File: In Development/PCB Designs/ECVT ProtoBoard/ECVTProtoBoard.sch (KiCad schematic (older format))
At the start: 26 parts, among them J1 Motor Driver, J10 3V3, J11 GND, J12 Hall Effect, J13 Hall Effect 2, J14 12V In, J15 Conn_01x08, J16 MotorDriver2, J17 GND In, J2 Conn_01x01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

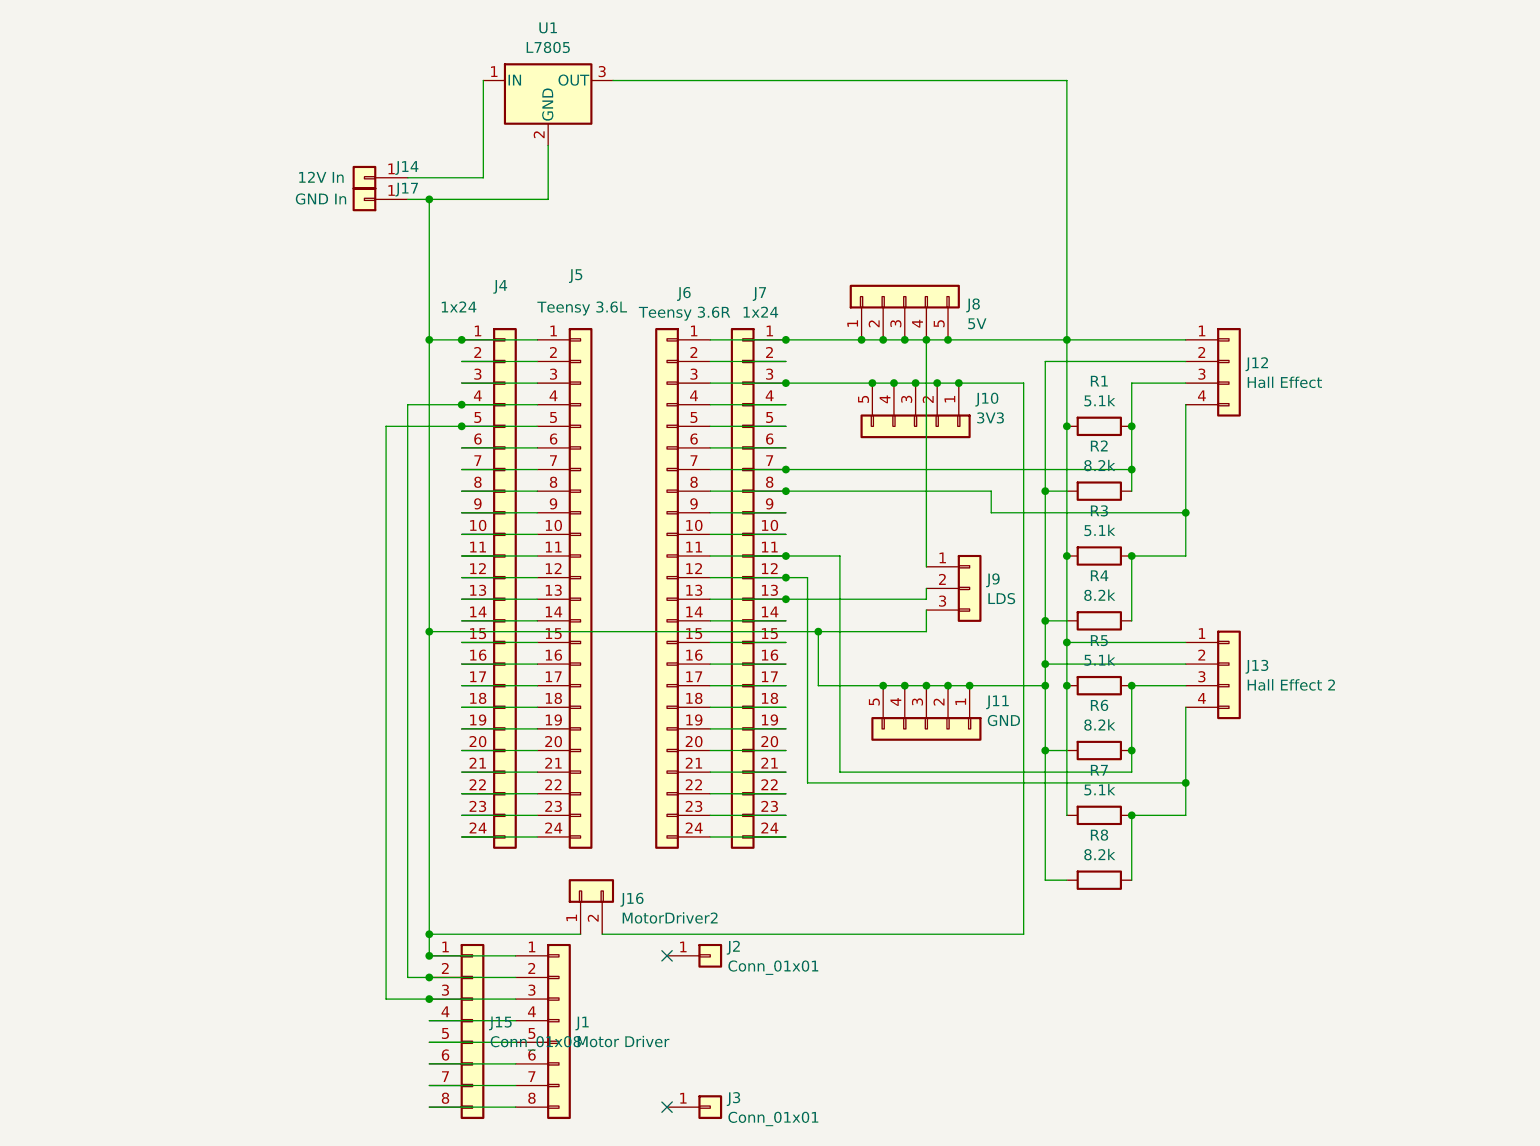
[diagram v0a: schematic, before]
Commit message: Finished eCVT protoboard schematic
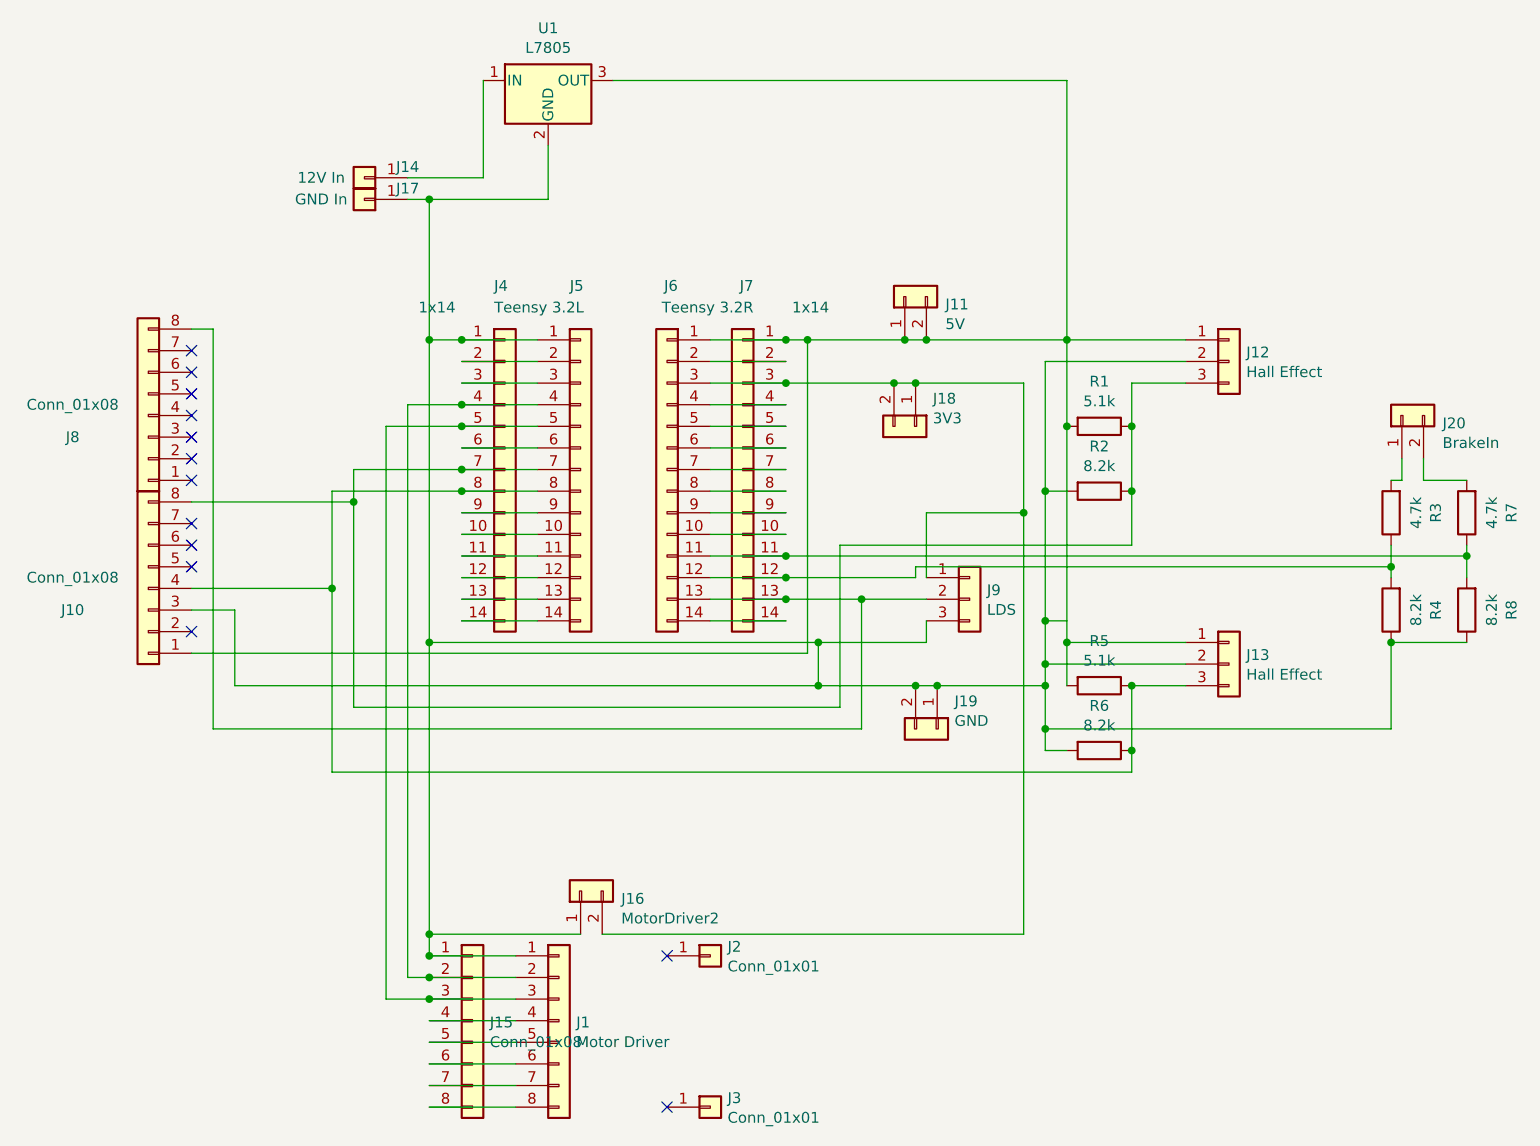
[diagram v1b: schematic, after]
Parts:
- removed J10: 3V3, Connector_PinHeader_2.54mm:PinHeader_1x05_P2.54mm_Vertical, symbol Connector_Generic:Conn_01x05
- removed J11: GND, Connector_PinHeader_2.54mm:PinHeader_1x05_P2.54mm_Vertical, symbol Connector_Generic:Conn_01x05
- removed J12: Hall Effect, Connector_PinHeader_2.54mm:PinHeader_1x04_P2.54mm_Vertical, symbol Connector_Generic:Conn_01x04
- removed J13: Hall Effect 2, Connector_PinHeader_2.54mm:PinHeader_1x04_P2.54mm_Vertical, symbol Connector_Generic:Conn_01x04
- removed J4, J7: 1x24, Connector_PinHeader_2.54mm:PinHeader_1x24_P2.54mm_Vertical, symbol Connector_Generic:Conn_01x24
- removed J5: Teensy 3.6L, Connector_PinHeader_2.54mm:PinHeader_1x24_P2.54mm_Vertical, symbol Connector_Generic:Conn_01x24
- removed J6: Teensy 3.6R, Connector_PinHeader_2.54mm:PinHeader_1x24_P2.54mm_Vertical, symbol Connector_Generic:Conn_01x24
- removed J8: 5V, Connector_PinHeader_2.54mm:PinHeader_1x05_P2.54mm_Vertical, symbol Connector_Generic:Conn_01x05
- added J10, J8: Conn_01x08, Connector_PinHeader_2.00mm:PinHeader_1x08_P2.00mm_Vertical, symbol Connector_Generic:Conn_01x08
- added J11: 5V, Connector_PinHeader_2.54mm:PinHeader_1x02_P2.54mm_Vertical, symbol Connector_Generic:Conn_01x02
- added J12, J13: Hall Effect, Connector_PinHeader_2.54mm:PinHeader_1x03_P2.54mm_Vertical, symbol Connector_Generic:Conn_01x03
- added J18: 3V3, Connector_PinHeader_2.54mm:PinHeader_1x02_P2.54mm_Vertical, symbol Connector_Generic:Conn_01x02
- added J19: GND, Connector_PinHeader_2.54mm:PinHeader_1x02_P2.54mm_Vertical, symbol Connector_Generic:Conn_01x02
- added J20: BrakeIn, Connector_PinHeader_2.54mm:PinHeader_1x02_P2.54mm_Vertical, symbol Connector_Generic:Conn_01x02
- added J4, J7: 1x14, Connector_PinHeader_2.54mm:PinHeader_1x14_P2.54mm_Vertical, symbol Connector_Generic:Conn_01x14
- added J5: Teensy 3.2L, Connector_PinHeader_2.54mm:PinHeader_1x14_P2.54mm_Vertical, symbol Connector_Generic:Conn_01x14
- added J6: Teensy 3.2R, Connector_PinHeader_2.54mm:PinHeader_1x14_P2.54mm_Vertical, symbol Connector_Generic:Conn_01x14
- R3, R7: value 5.1k -> 4.7k
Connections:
- net at R1.2, R5.2, U1.3 (OUT): now also J10.1 (Pin_1), J11.1 (Pin_1), J11.2 (Pin_2), J12.1 (Pin_1), J13.1 (Pin_1), J6.1 (Pin_1), J7.1 (Pin_1); no longer J9.1 (Pin_1), R3.2, R7.2
- net at J9.2 (Pin_2): now also J6.13 (Pin_13), J7.13 (Pin_13), J8.8 (Pin_8)
- net at J1.1 (Pin_1), J15.1 (Pin_1), J16.1 (Pin_1)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: now also R4.1, R8.1, J10.3 (Pin_3), J12.2 (Pin_2), J13.2 (Pin_2), J19.1 (Pin_1), J19.2 (Pin_2), J4.1 (Pin_1), J5.1 (Pin_1); no longer R4.2, R8.2
- net at J1.2 (Pin_2), J15.2 (Pin_2): now also J4.4 (Pin_4), J5.4 (Pin_4)
- net at J1.3 (Pin_3), J15.3 (Pin_3): now also J4.5 (Pin_5), J5.5 (Pin_5)
- net at R1.1, R2.1: now also J10.8 (Pin_8), J12.3 (Pin_3), J4.7 (Pin_7), J5.7 (Pin_7)
- net at R3.1: now also R4.2, J6.12 (Pin_12), J7.12 (Pin_12); no longer R4.1
- net at R5.1, R6.1: now also J10.4 (Pin_4), J13.3 (Pin_3), J4.8 (Pin_8), J5.8 (Pin_8)
- net at R7.1: now also R8.2, J6.11 (Pin_11), J7.11 (Pin_11); no longer R8.1
- net at J16.2 (Pin_2): now also J9.1 (Pin_1), J18.1 (Pin_1), J18.2 (Pin_2), J6.3 (Pin_3), J7.3 (Pin_3)
- new net: J4.10 (Pin_10), J5.10 (Pin_10)
- new net: J4.11 (Pin_11), J5.11 (Pin_11)
- new net: J4.12 (Pin_12), J5.12 (Pin_12)
- new net: J4.13 (Pin_13), J5.13 (Pin_13)
- new net: J4.14 (Pin_14), J5.14 (Pin_14)
- new net: J4.2 (Pin_2), J5.2 (Pin_2)
- new net: J4.3 (Pin_3), J5.3 (Pin_3)
- new net: J4.6 (Pin_6), J5.6 (Pin_6)
- new net: J4.9 (Pin_9), J5.9 (Pin_9)
- new net: J6.10 (Pin_10), J7.10 (Pin_10)
- new net: J6.14 (Pin_14), J7.14 (Pin_14)
- new net: J6.2 (Pin_2), J7.2 (Pin_2)
- new net: J6.4 (Pin_4), J7.4 (Pin_4)
- new net: J6.5 (Pin_5), J7.5 (Pin_5)
- new net: J6.6 (Pin_6), J7.6 (Pin_6)
- new net: J6.7 (Pin_7), J7.7 (Pin_7)
- new net: J6.8 (Pin_8), J7.8 (Pin_8)
- new net: J6.9 (Pin_9), J7.9 (Pin_9)
- new net: J20.1 (Pin_1), R3.2
- new net: J20.2 (Pin_2), R7.2
- no-connect marks 2 -> 13
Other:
- moved on the sheet: J9

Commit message: Finished eCVT PCB rev 2
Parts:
- removed J14: 12V In, Connector_PinHeader_2.54mm:PinHeader_1x01_P2.54mm_Vertical, symbol Connector_Generic:Conn_01x01
- removed J17: GND In, Connector_PinHeader_2.54mm:PinHeader_1x01_P2.54mm_Vertical, symbol Connector_Generic:Conn_01x01
- added J14: External Power Switch, Connector_PinHeader_2.54mm:PinHeader_2x03_P2.54mm_Vertical, symbol Connector_Generic:Conn_02x03_Top_Bottom
- J12, J13, J9: footprint Connector_PinHeader_2.54mm:PinHeader_1x03_P2.54mm_Vertical -> CustomKiCADLibrary:PinHeader_1x03_P5.08mm_Vertical
- J20: footprint Connector_PinHeader_2.54mm:PinHeader_1x02_P2.54mm_Vertical -> CustomKiCADLibrary:PinHeader_1x02_P5.08mm_Vertical
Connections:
- net at J1.6 (Pin_6), J15.6 (Pin_6): now also J6.12 (Pin_12), J7.12 (Pin_12), J8.1 (Pin_1)
- net at J1.8 (Pin_8), J15.8 (Pin_8): now also U1.1 (IN)
- net at J10.1 (Pin_1), J11.1 (Pin_1), J11.2 (Pin_2)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: now also J14.3 (Pin_3); no longer U1.3 (OUT)
- net at J8.3 (Pin_3): now also J6.11 (Pin_11), J7.11 (Pin_11), R3.1, R4.2
- net at J8.4 (Pin_4): now also J6.10 (Pin_10), J7.10 (Pin_10), R7.1, R8.2
- new net: J14.1 (Pin_1), U1.3 (OUT)
- no-connect marks 13 -> 14
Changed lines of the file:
@@
 	4300 6200 4700 6200
-Wire Wire Line
-	4300 6300 4700 6300
 Wire Wire Line
 	4300 6400 4700 6400
@@
 $EndComp
 Wire Wire Line
-	4200 2200 4550 2200
-Wire Wire Line
-	4550 2200 4550 1750
-Wire Wire Line
-	4200 2300 4300 2300
-Wire Wire Line
 	4850 2300 4850 2050
 Wire Wire Line
 	4300 2300 4300 2950
-Connection ~ 4300 2300
 Wire Wire Line
 	4300 2300 4850 2300
@@
 Connection ~ 7550 3350
 Wire Wire Line
-	7250 1750 7250 2950
+	7250 1750 7250 2000
 $Comp
 L Device:R R5
@@
 Wire Wire Line
 	7150 4850 7250 4850
-Wire Wire Line
-	7150 4250 7250 4250
-Connection ~ 7150 4250
-Wire Wire Line
-	7150 4250 7150 3650
 Connection ~ 7250 3350
 Wire Wire Line
@@
 Connection ~ 7150 4450
 Wire Wire Line
-	7150 4450 7150 4250
-Wire Wire Line
 	7800 4550 7550 4550
 Wire Wire Line
@@
 	7550 4950 7550 4850
 Connection ~ 7550 4850
-$Comp
-L Connector_Generic:Conn_01x01 J14
-U 1 1 5DDB2E37
-P 4000 2200
-F 0 "J14" H 3800 2150 50  0000 C CNN
-F 1 "12V In" H 4200 2200 50  0000 C CNN
-F 2 "Connector_PinHeader_2.54mm:PinHeader_1x01_P2.54mm_Vertical" H 4000 2200 50  0001 C CNN
-F 3 "~" H 4000 2200 50  0001 C CNN
-	1    4000 2200
-	-1   0    0    1
-$EndComp
-$Comp
-L Connector_Generic:Conn_01x01 J17
-U 1 1 5DDB375B
-P 4000 2300
-F 0 "J17" H 3800 2250 50  0000 C CNN
-F 1 "GND In" H 4200 2300 50  0000 C CNN
-F 2 "Connector_PinHeader_2.54mm:PinHeader_1x01_P2.54mm_Vertical" H 4000 2300 50  0001 C CNN
-F 3 "~" H 4000 2300 50  0001 C CNN
-	1    4000 2300
-	-1   0    0    1
-$EndComp
 Wire Wire Line
 	7250 3350 7250 4350
@@
 F 0 "J12" H 8080 3092 50  0000 L CNN
 F 1 "Hall Effect" H 8080 3001 50  0000 L CNN
-F 2 "Connector_PinHeader_2.54mm:PinHeader_1x03_P2.54mm_Vertical" H 8000 3050 50  0001 C CNN
+F 2 "CustomKiCADLibrary:PinHeader_1x03_P5.08mm_Vertical" H 8000 3050 50  0001 C CNN
 F 3 "~" H 8000 3050 50  0001 C CNN
 	1    8000 3050
@@
 F 0 "J13" H 8080 4492 50  0000 L CNN
 F 1 "Hall Effect" H 8080 4401 50  0000 L CNN
-F 2 "Connector_PinHeader_2.54mm:PinHeader_1x03_P2.54mm_Vertical" H 8000 4450 50  0001 C CNN
+F 2 "CustomKiCADLibrary:PinHeader_1x03_P5.08mm_Vertical" H 8000 4450 50  0001 C CNN
 F 3 "~" H 8000 4450 50  0001 C CNN
 	1    8000 4450
@@
 F 0 "J9" H 6880 4192 50  0000 L CNN
 F 1 "LDS" H 6880 4101 50  0000 L CNN
-F 2 "Connector_PinHeader_2.54mm:PinHeader_1x03_P2.54mm_Vertical" H 6800 4150 50  0001 C CNN
+F 2 "CustomKiCADLibrary:PinHeader_1x03_P5.08mm_Vertical" H 6800 4150 50  0001 C CNN
 F 3 "~" H 6800 4150 50  0001 C CNN
 	1    6800 4150
@@
 Wire Wire Line
 	6300 4150 6600 4150
-NoConn ~ 3200 3300
-NoConn ~ 3200 3400
-NoConn ~ 3200 3600
 Wire Wire Line
 	6300 4750 3300 4750
@@
 F 0 "J20" V 8764 3112 50  0000 R CNN
 F 1 "BrakeIn" V 8673 3112 50  0000 R CNN
-F 2 "Connector_PinHeader_2.54mm:PinHeader_1x02_P2.54mm_Vertical" H 8800 3300 50  0001 C CNN
+F 2 "CustomKiCADLibrary:PinHeader_1x02_P5.08mm_Vertical" H 8800 3300 50  0001 C CNN
 F 3 "~" H 8800 3300 50  0001 C CNN
 	1    8800 3300
@@
 Wire Wire Line
 	8750 3900 8750 4000
+Connection ~ 8750 4000
+Wire Wire Line
+	8750 4000 8750 4050
 Wire Wire Line
 	9100 3900 9100 3950
 Wire Wire Line
-	5950 4050 6550 4050
-Wire Wire Line
-	6550 4050 6550 4000
-Wire Wire Line
-	6550 4000 8750 4000
+	6450 4000 6450 3950
+Wire Wire Line
+	6450 3950 5950 3950
+Wire Wire Line
+	6450 4000 8450 4000
+Connection ~ 5950 3950
+Wire Wire Line
+	7800 3850 5950 3850
+Connection ~ 5950 3850
+Wire Wire Line
+	5950 4050 6000 4050
+Wire Wire Line
+	6000 4050 6000 5400
+Wire Wire Line
+	6000 5400 4000 5400
+Wire Wire Line
+	4000 5400 4000 6300
+Wire Wire Line
+	4000 6300 4300 6300
 Connection ~ 5950 4050
-Connection ~ 8750 4000
-Wire Wire Line
-	8750 4000 8750 4050
-Wire Wire Line
-	5950 3950 9100 3950
-Connection ~ 5950 3950
+Connection ~ 4300 6300
+Wire Wire Line
+	4300 6300 4700 6300
+Wire Wire Line
+	4300 6500 3800 6500
+Wire Wire Line
+	3800 6500 3800 1750
+Wire Wire Line
+	3800 1750 4550 1750
+Connection ~ 4300 6500
+Wire Wire Line
+	7800 3950 8600 3950
+Wire Wire Line
+	7800 3850 7800 3950
 Connection ~ 9100 3950
 Wire Wire Line
 	9100 3950 9100 4050
+Wire Wire Line
+	8450 4000 8450 2600
+Wire Wire Line
+	8450 2600 3550 2600
+Wire Wire Line
+	3550 2600 3550 3400
+Wire Wire Line
+	3550 3400 3200 3400
+Connection ~ 8450 4000
+Wire Wire Line
+	8450 4000 8750 4000
+Wire Wire Line
+	8600 3950 8600 2500
+Wire Wire Line
+	8600 2500 3450 2500
+Wire Wire Line
+	3450 2500 3450 3300
+Wire Wire Line
+	3450 3300 3200 3300
+Connection ~ 8600 3950
+Wire Wire Line
+	8600 3950 9100 3950
+Wire Wire Line
+	4000 6300 3600 6300
+Wire Wire Line
+	3600 6300 3600 3600
+Wire Wire Line
+	3600 3600 3200 3600
+Connection ~ 4000 6300
+$Comp
+L Connector_Generic:Conn_02x03_Top_Bottom J14
+U 1 1 5E32A8A1
+P 7450 2100
+F 0 "J14" H 7500 2417 50  0000 C CNN
+F 1 "External Power Switch" H 7500 2326 50  0000 C CNN
+F 2 "Connector_PinHeader_2.54mm:PinHeader_2x03_P2.54mm_Vertical" H 7450 2100 50  0001 C CNN
+F 3 "~" H 7450 2100 50  0001 C CNN
+	1    7450 2100
+	1    0    0    -1
+$EndComp
+NoConn ~ 7750 2000
+NoConn ~ 7750 2100
+NoConn ~ 7750 2200
+Wire Wire Line
+	7250 2200 7250 2950
+NoConn ~ 7250 2100
+Wire Wire Line
+	7150 3650 7150 4450
 $EndSCHEMATC

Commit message: Finished DAQ board and ready for initial production
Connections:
- net at J1.1 (Pin_1), J12.2 (Pin_2), J13.2 (Pin_2)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: now also J8.1 (Pin_1); no longer J10.3 (Pin_3)
- net at J1.6 (Pin_6), J15.6 (Pin_6), J6.12 (Pin_12)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: no longer J8.1 (Pin_1)
- net at J11.1 (Pin_1), J11.2 (Pin_2), J12.1 (Pin_1)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: no longer J10.1 (Pin_1)
- net at J4.10 (Pin_10), J5.10 (Pin_10): now also J10.3 (Pin_3)
- net at J4.9 (Pin_9), J5.9 (Pin_9): now also J10.1 (Pin_1)
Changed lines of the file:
@@
 	4450 3350 4800 3350
 Connection ~ 5950 2950
-Wire Wire Line
-	5950 2950 6050 2950
 Connection ~ 5950 3150
 Connection ~ 5950 4150
@@
 NoConn ~ 3200 3000
 Wire Wire Line
-	6050 2950 6050 4400
-Wire Wire Line
-	6050 4400 3200 4400
-Connection ~ 6050 2950
-Wire Wire Line
-	6100 4550 3400 4550
-Wire Wire Line
-	3400 4550 3400 4200
-Wire Wire Line
-	3400 4200 3200 4200
+	6100 4550 3600 4550
 Connection ~ 6100 4550
 Wire Wire Line
@@
 	-1   0    0    1
 $EndComp
-Wire Wire Line
-	6050 2950 6500 2950
 $Comp
 L Connector_Generic:Conn_01x02 J11
@@
 	8600 3950 9100 3950
 Wire Wire Line
-	4000 6300 3600 6300
-Wire Wire Line
-	3600 6300 3600 3600
-Wire Wire Line
 	3600 3600 3200 3600
-Connection ~ 4000 6300
 $Comp
 L Connector_Generic:Conn_02x03_Top_Bottom J14
@@
 Wire Wire Line
 	7150 3650 7150 4450
+Wire Wire Line
+	3600 3600 3600 4550
+Wire Wire Line
+	5950 2950 6500 2950
+Wire Wire Line
+	3200 4200 4350 4200
+Wire Wire Line
+	3200 4400 4400 4400
+Wire Wire Line
+	4350 4200 4350 3850
+Wire Wire Line
+	4350 3850 4450 3850
+Connection ~ 4450 3850
+Wire Wire Line
+	4400 4400 4400 3750
+Wire Wire Line
+	4400 3750 4450 3750
+Connection ~ 4450 3750
 $EndSCHEMATC
